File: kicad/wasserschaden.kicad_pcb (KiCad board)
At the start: 2 copper layers, 50.8 x 50.2 mm, 13 parts, among them J1 valve out, J2 12V in, U1 stepdown, U2 WeMos_mini

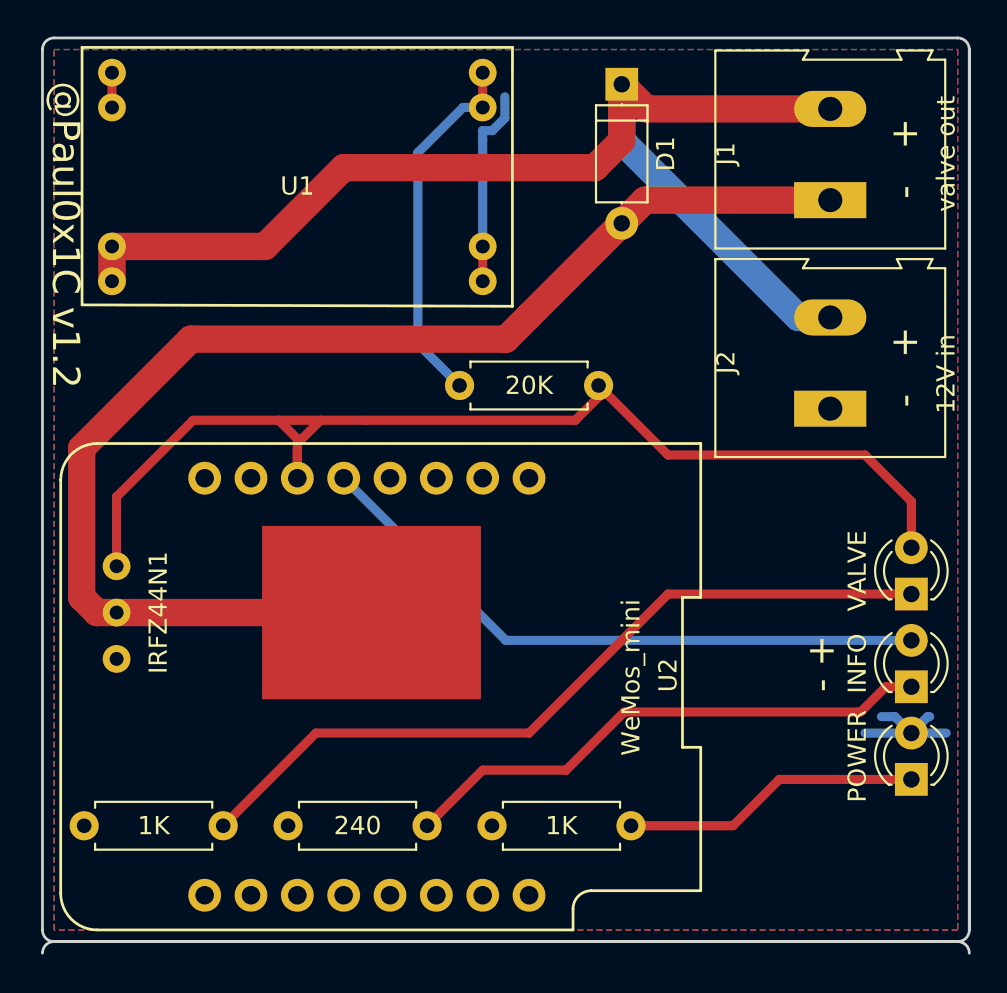
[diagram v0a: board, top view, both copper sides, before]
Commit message: added jumper to pcb
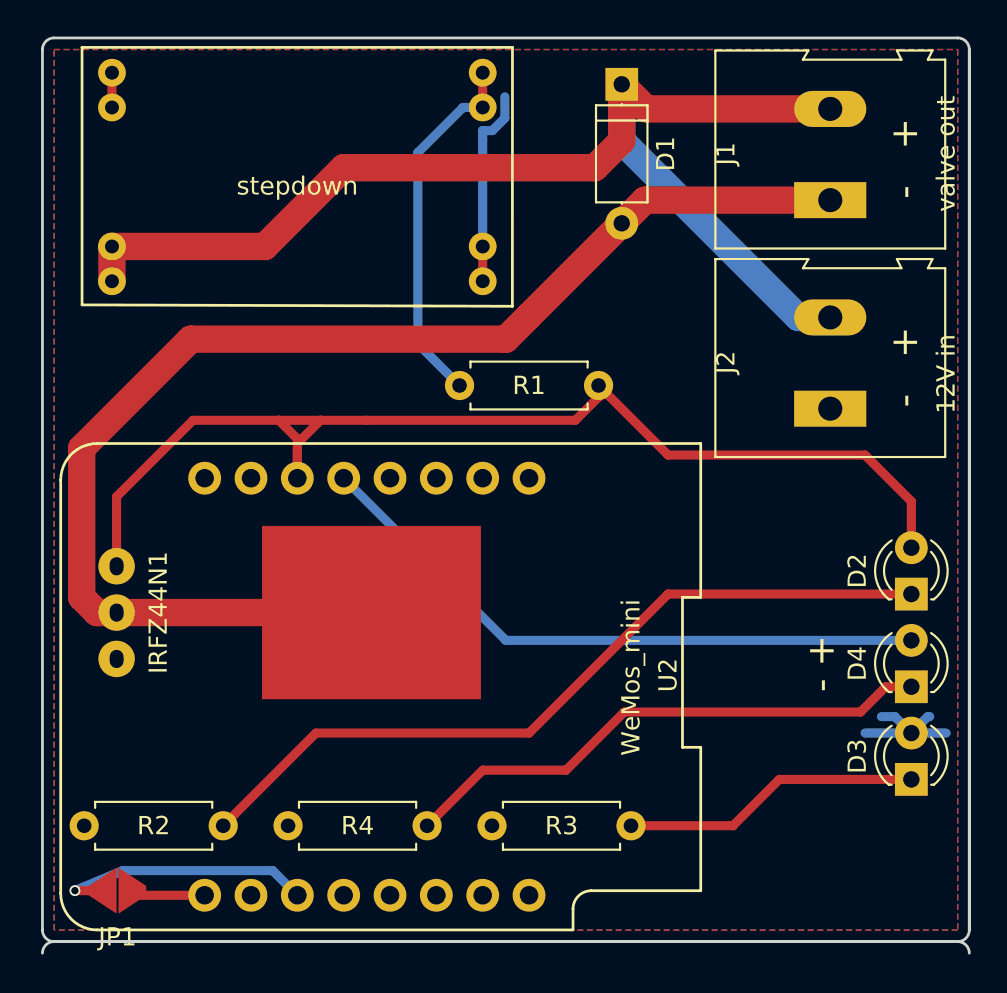
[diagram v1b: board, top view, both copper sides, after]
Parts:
- removed U1: stepdown, stepdown:stepdown
- added JP1: SolderJumper_2_Open, custom:jumper, F.Cu at (129.8, 105.2)
- added stepdown: stepdown, custom:stepdown, F.Cu at (139.7, 66.0)
- IRFZ44N1: footprint test_wemos:irlz44n -> custom:irlz44n
- U2: footprint test_wemos:wemos-d1-mini-with-pin-header -> custom:wemos
- renumbered VALVE to D2, POWER to D3, INFO to D4, 20K to R1, 1K to R2, 1K to R3, 240 to R4
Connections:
- D3 pad 2: +3V3 -> Net-(D3-Pad2)
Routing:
- net Net-(JP1-Pad1): track 0.00 -> 14.5 mm, vias 0 -> 1
- net Net-(D3-Pad2): track 0.00 -> 7.84 mm
- net +3V3: track 18.8 -> 10.9 mm
- net Net-(JP1-Pad2): track 0.00 -> 4.07 mm
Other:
- board text removed: "@Paul0x1C v1.2"
